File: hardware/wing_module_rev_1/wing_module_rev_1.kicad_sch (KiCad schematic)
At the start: 22 parts, among them J1 Conn_01x03, J2 Conn_01x03, J3 Conn_ST_STDC14, J4 Conn_01x04, U1 STM32F103T8U6

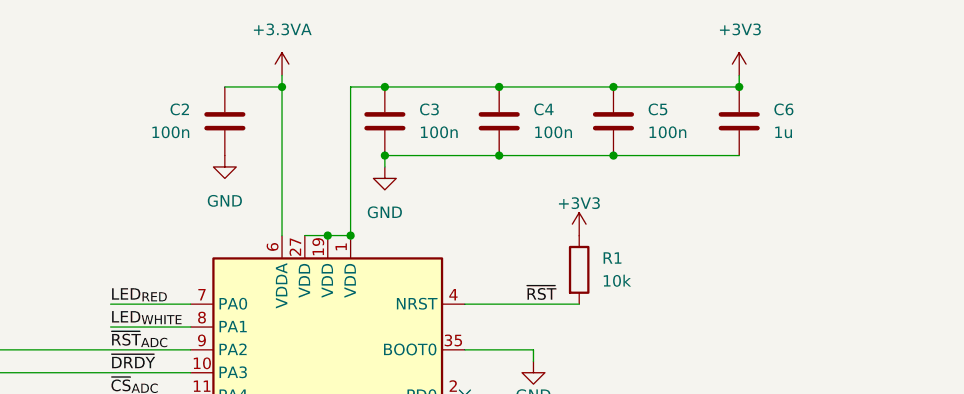
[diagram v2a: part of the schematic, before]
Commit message: Reassigned reference numbers
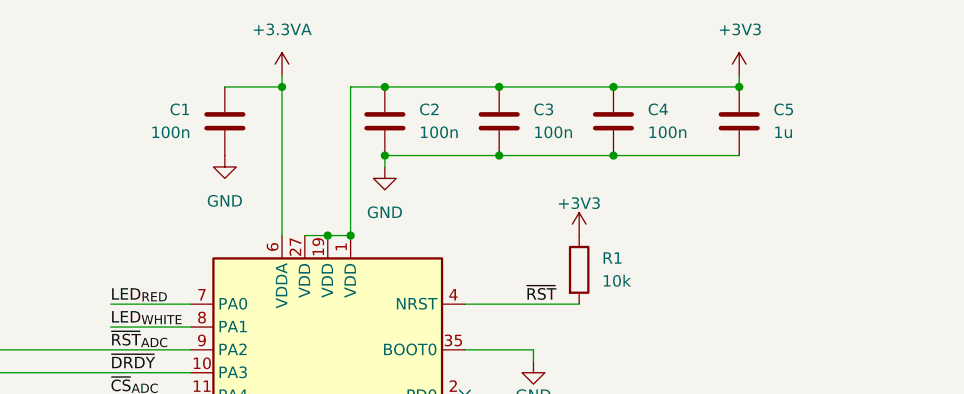
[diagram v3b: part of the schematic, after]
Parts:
- renumbered C2 to C1, C3 to C2, C4 to C3, C5 to C4, C6 to C5
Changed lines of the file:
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@@
 		(dnp no)
 		(fields_autoplaced yes)
-		(property "Reference" "C4"
+		(property "Reference" "C3"
 			(at 168.91 33.0199 0)
 			(effects
@@
 			(project "wing_module_rev_1"
 				(path "/7b7fffa9-e888-4279-94bf-385d74cf78f9"
-					(reference "C4")
+					(reference "C3")
 					(unit 1)
 				)
@@
 		(dnp no)
 		(fields_autoplaced yes)
-		(property "Reference" "C5"
+		(property "Reference" "C4"
 			(at 181.61 33.0199 0)
 			(effects
@@
 			(project "wing_module_rev_1"
 				(path "/7b7fffa9-e888-4279-94bf-385d74cf78f9"
-					(reference "C5")
+					(reference "C4")
 					(unit 1)
 				)
@@
 		(dnp no)
 		(fields_autoplaced yes)
-		(property "Reference" "C2"
+		(property "Reference" "C1"
 			(at 130.81 33.0199 0)
 			(effects
@@
 			(project "wing_module_rev_1"
 				(path "/7b7fffa9-e888-4279-94bf-385d74cf78f9"
-					(reference "C2")
+					(reference "C1")
 					(unit 1)
 				)
@@
 		(on_board yes)
 		(dnp no)
-		(property "Reference" "C6"
+		(property "Reference" "C5"
 			(at 195.58 33.0199 0)
 			(effects
@@
 			(project "wing_module_rev_1"
 				(path "/7b7fffa9-e888-4279-94bf-385d74cf78f9"
-					(reference "C6")
+					(reference "C5")
 					(unit 1)
 				)
@@
 		(dnp no)
 		(fields_autoplaced yes)
-		(property "Reference" "C3"
+		(property "Reference" "C2"
 			(at 156.21 33.0199 0)
 			(effects
@@
 			(project "wing_module_rev_1"
 				(path "/7b7fffa9-e888-4279-94bf-385d74cf78f9"
-					(reference "C3")
-					(unit 1)
-				)
+					(reference "C2")
+					(unit 1)
+				)
